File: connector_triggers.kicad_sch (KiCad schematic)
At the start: 5 parts, among them J2 JST_SH_1x6_BM06B-SRSS-TB-LF-SN, U10 TPD4E02B04DQA

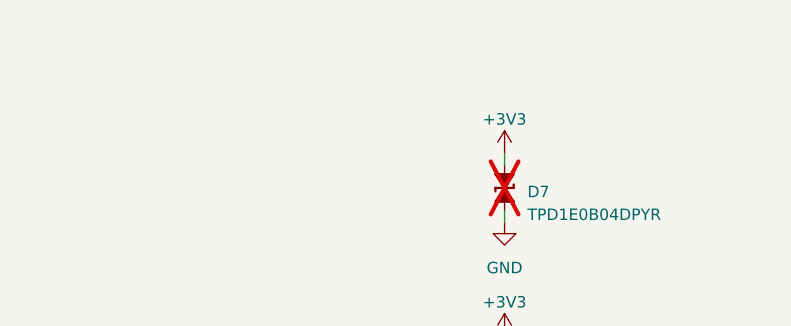
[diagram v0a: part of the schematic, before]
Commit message: [#72133] Add captions to schematic sheets
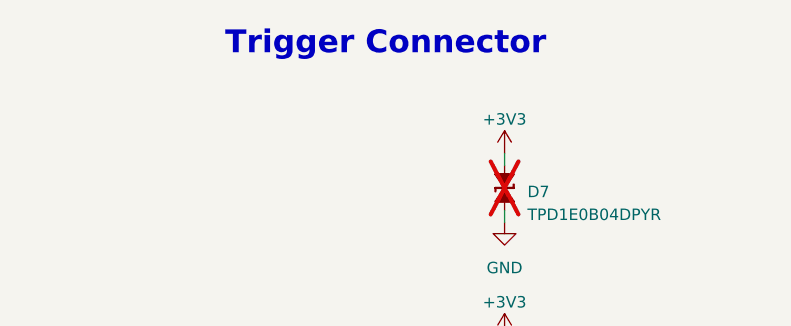
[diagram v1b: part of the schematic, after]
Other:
- note added: "Trigger Connector"
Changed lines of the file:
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@@
+		)
+	)
+	(text "Trigger Connector"
+		(exclude_from_sim no)
+		(at 141.732 47.498 0)
+		(effects
+			(font
+				(size 2.54 2.54)
+				(thickness 0.508)
+				(bold yes)
+			)
 		)
 	)

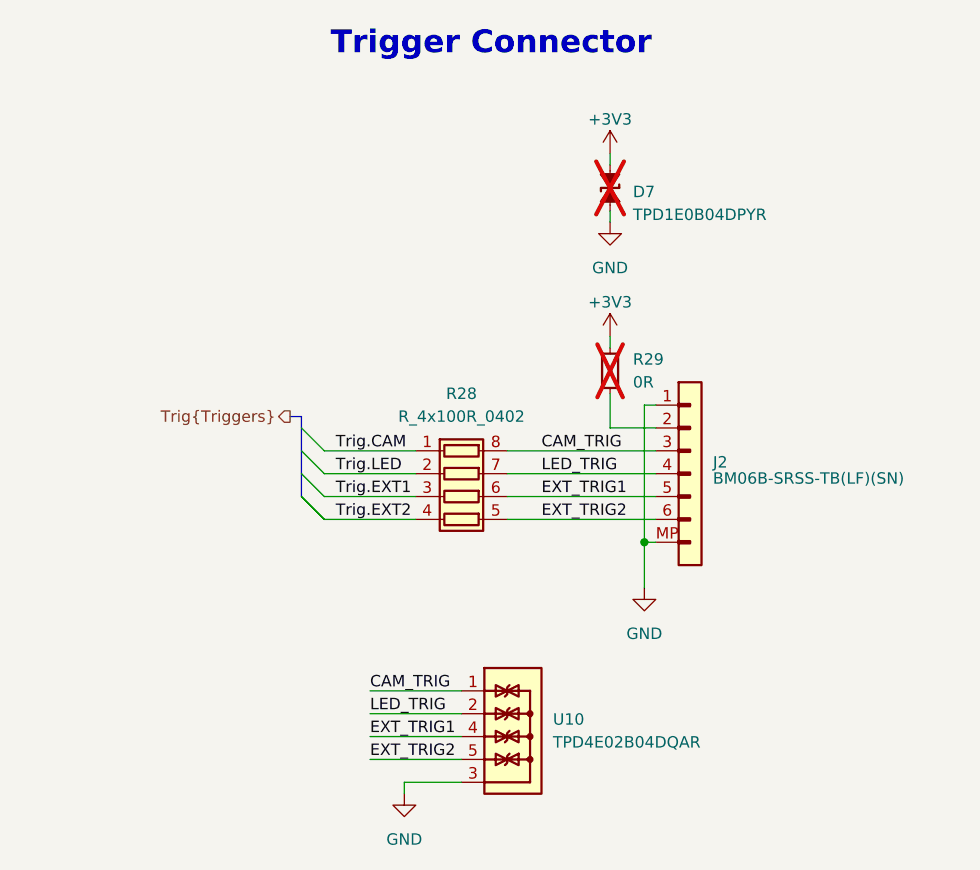
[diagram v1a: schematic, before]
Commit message: [#72133] Update trigger connectors sheet
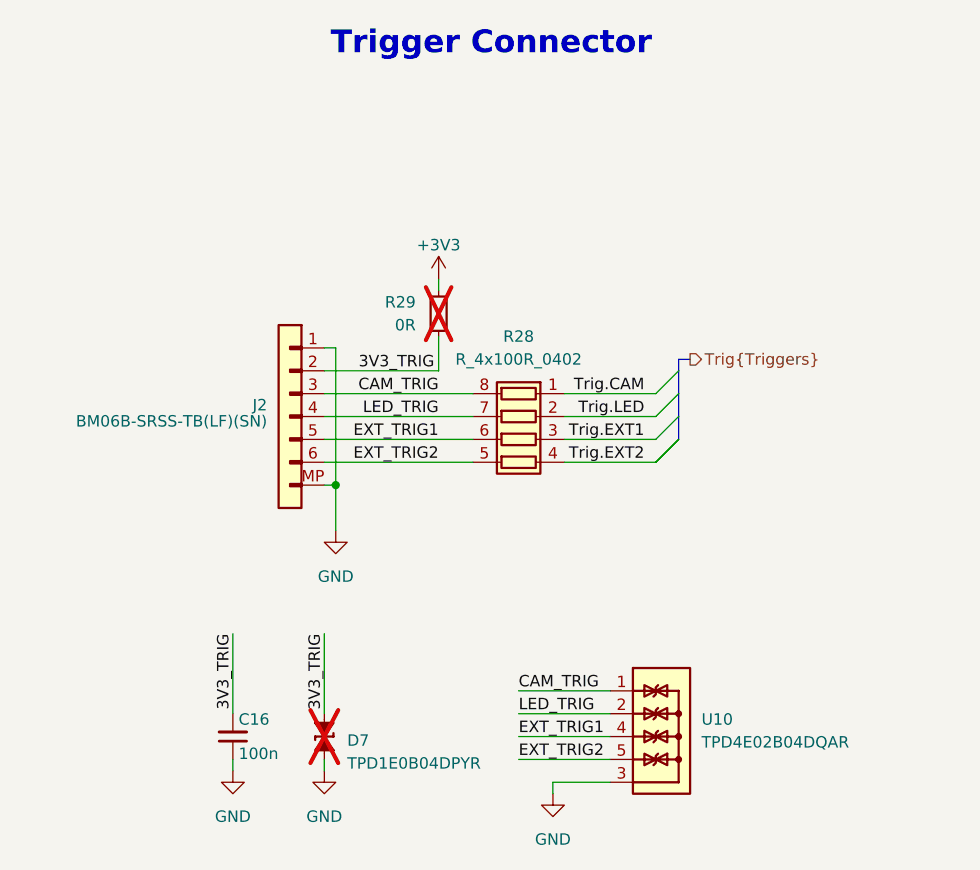
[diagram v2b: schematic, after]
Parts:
- added C16: C_100n_0402, antmicro-footprints:C_0402_1005Metric, symbol antmicroCapacitors0402:C_100n_0402
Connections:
- net +3V3: no longer D7.1 (C)
- net GND: now also C16.1
- net 3V3_TRIG: now reaches J2.2, R29.1
- net 3V3_TRIG: now also D7.1 (C), C16.2
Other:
- moved on the sheet: D7, J2, R28, R29, U10

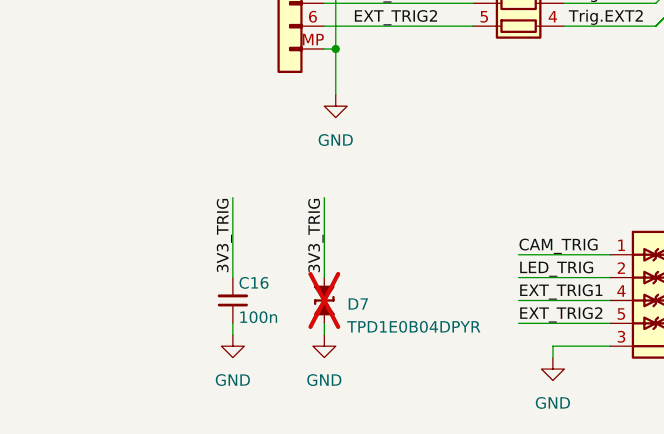
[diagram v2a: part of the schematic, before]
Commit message: [#72133] Clean ERC
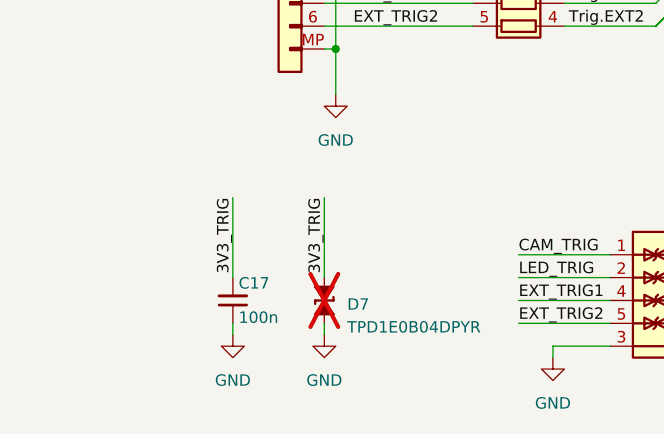
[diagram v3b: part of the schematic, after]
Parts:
- renumbered C16 to C17
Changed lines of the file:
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@@
 		(dnp no)
 		(fields_autoplaced yes)
-		(property "Reference" "#PWR038"
+		(property "Reference" "#PWR039"
 			(at 121.92 130.81 0)
 			(effects
@@
 		(on_board yes)
 		(dnp no)
-		(property "Reference" "C16"
+		(property "Reference" "C17"
 			(at 113.665 122.555 90)
 			(effects

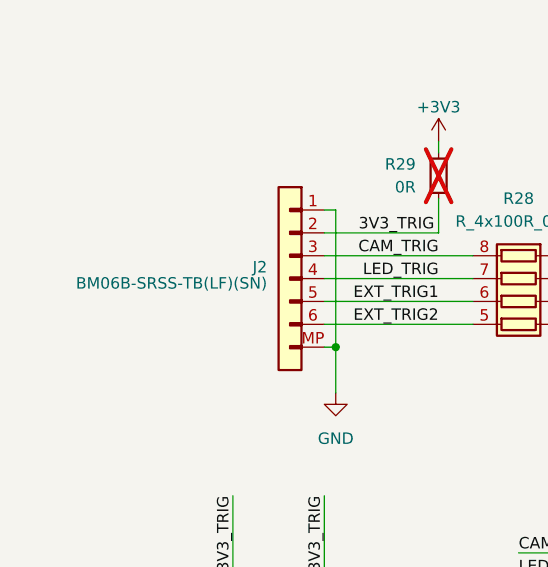
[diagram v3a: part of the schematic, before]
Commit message: [#72447] Change connectors to horizontal
Signed-off-by: Dawid Lentka <dlentka@antmicro.com>
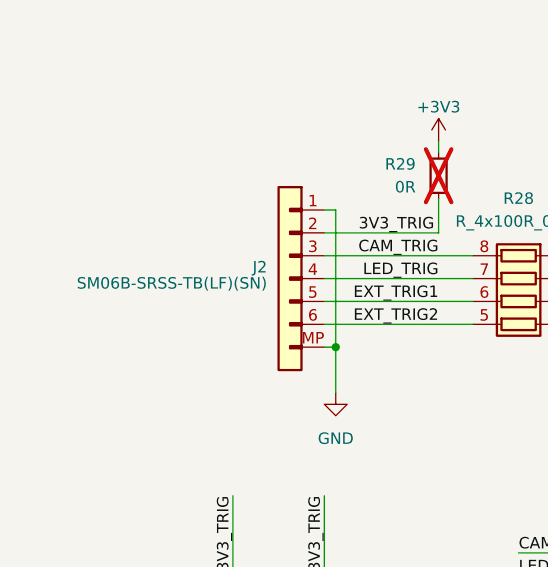
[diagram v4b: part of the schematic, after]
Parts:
- J2: value JST_SH_1x6_BM06B-SRSS-TB-LF-SN -> JST_SH_1x6_SM06B-SRSS-TB-LF-SN; footprint antmicro-footprints:Conn_JST_SH_1x6_BM06B-SRSS-TB-LF-SN -> antmicro-footprints:Conn_JST_SH_1x6_SM06B-SRSS-TB-LF-SN; symbol antmicroWire2BoardConnectors:JST_SH_1x6_BM06B-SRSS-TB-LF-SN -> antmicroWire2BoardConnectors:JST_SH_1x6_SM06B-SRSS-TB-LF-SN; MPN BM06B-SRSS-TB(LF)(SN) -> SM06B-SRSS-TB(LF)(SN)
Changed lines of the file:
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@@
 	)
 	(symbol
-		(lib_id "antmicroWire2BoardConnectors:JST_SH_1x6_BM06B-SRSS-TB-LF-SN")
+		(lib_id "antmicroWire2BoardConnectors:JST_SH_1x6_SM06B-SRSS-TB-LF-SN")
 		(at 123.19 81.28 0)
 		(mirror y)
@@
 			)
 		)
-		(property "Value" "JST_SH_1x6_BM06B-SRSS-TB-LF-SN"
+		(property "Value" "JST_SH_1x6_SM06B-SRSS-TB-LF-SN"
 			(at 102.87 88.9 0)
 			(effects
@@
 			)
 		)
-		(property "Footprint" "antmicro-footprints:Conn_JST_SH_1x6_BM06B-SRSS-TB-LF-SN"
+		(property "Footprint" "antmicro-footprints:Conn_JST_SH_1x6_SM06B-SRSS-TB-LF-SN"
 			(at 102.87 91.44 0)
 			(effects
@@
 			)
 		)
-		(property "Datasheet" "https://www.farnell.com/datasheets/2082363.pdf"
+		(property "Datasheet" "https://www.jst-mfg.com/product/pdf/eng/eSH.pdf"
 			(at 102.87 93.98 0)
 			(effects
@@
 			)
 		)
-		(property "Description" "Pin Header, Vertical, Wire-to-Board, 1 mm, 1 Rows, 6 Contacts, Surface Mount Straight, SH"
+		(property "Description" "Pin Header, Right Angle, Wire-to-Board, 1 mm, 1 Rows, 6 Contacts, Surface Mount Right Angle, SR"
 			(at 123.19 81.28 0)
 			(effects
@@
 			)
 		)
-		(property "MPN" "BM06B-SRSS-TB(LF)(SN)"
+		(property "MPN" "SM06B-SRSS-TB(LF)(SN)"
 			(at 116.84 90.17 0)
 			(effects

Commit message: [#72533] PCB: routing- WIP
Signed-off-by: Dawid Lentka <dlentka@antmicro.com>
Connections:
- net CAM_TRIG: now also R28.1 (R1.1); no longer R28.8 (R1.2)
- net EXT_TRIG1: now also R28.3 (R3.1); no longer R28.6 (R3.2)
- net EXT_TRIG2: now also R28.4 (R4.1); no longer R28.5 (R4.2)
- net LED_TRIG: now also R28.2 (R2.1); no longer R28.7 (R2.2)
- net Trig.CAM: now also R28.8 (R1.2); no longer R28.1 (R1.1)
- net Trig.EXT1: now also R28.6 (R3.2); no longer R28.3 (R3.1)
- net Trig.EXT2: now also R28.5 (R4.2); no longer R28.4 (R4.1)
- net Trig.LED: now also R28.7 (R2.2); no longer R28.2 (R2.1)
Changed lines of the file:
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@@
 	(symbol
 		(lib_id "antmicroResistorNetworksArrays:R_4x100R_0402_array")
-		(at 149.86 86.36 0)
-		(mirror y)
+		(at 139.7 86.36 0)
 		(unit 1)
 		(exclude_from_sim no)
@@
 		(on_board yes)
 		(dnp no)
-		(fields_autoplaced yes)
 		(property "Reference" "R28"
 			(at 144.78 80.01 0)
@@
 		)
 		(property "Value" "R_4x100R_0402_array"
-			(at 123.19 91.44 0)
+			(at 166.37 91.44 0)
 			(effects
 				(font
@@
 		)
 		(property "Footprint" "antmicro-footprints:R_Array_4x0402_Panasonic_EXB28V"
-			(at 123.19 96.52 0)
+			(at 166.37 96.52 0)
 			(effects
 				(font
@@
 		)
 		(property "Datasheet" "http://industrial.panasonic.com/cdbs/www-data/pdf/AOC0000/AOC0000C14.pdf"
-			(at 123.19 99.06 0)
+			(at 166.37 99.06 0)
 			(effects
 				(font
@@
 		)
 		(property "Description" "Fixed Network Resistor, 100 ohm, Isolated, 4 Resistors, 0804 [2010 Metric], Convex, ± 5%"
-			(at 149.86 86.36 0)
+			(at 139.7 86.36 0)
 			(effects
 				(font
@@
 		)
 		(property "MPN" "EXB-28V101JX"
-			(at 123.19 101.6 0)
+			(at 166.37 101.6 0)
 			(effects
 				(font
@@
 		)
 		(property "Manufacturer" "Panasonic"
-			(at 123.19 104.14 0)
+			(at 166.37 104.14 0)
 			(effects
 				(font
@@
 		)
 		(property "Author" "Antmicro"
-			(at 123.19 106.68 0)
+			(at 166.37 106.68 0)
 			(effects
 				(font
@@
 		)
 		(property "License" "Apache-2.0"
-			(at 123.19 109.22 0)
+			(at 166.37 109.22 0)
 			(effects
 				(font
